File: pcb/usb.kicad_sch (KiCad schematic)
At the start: 4 parts

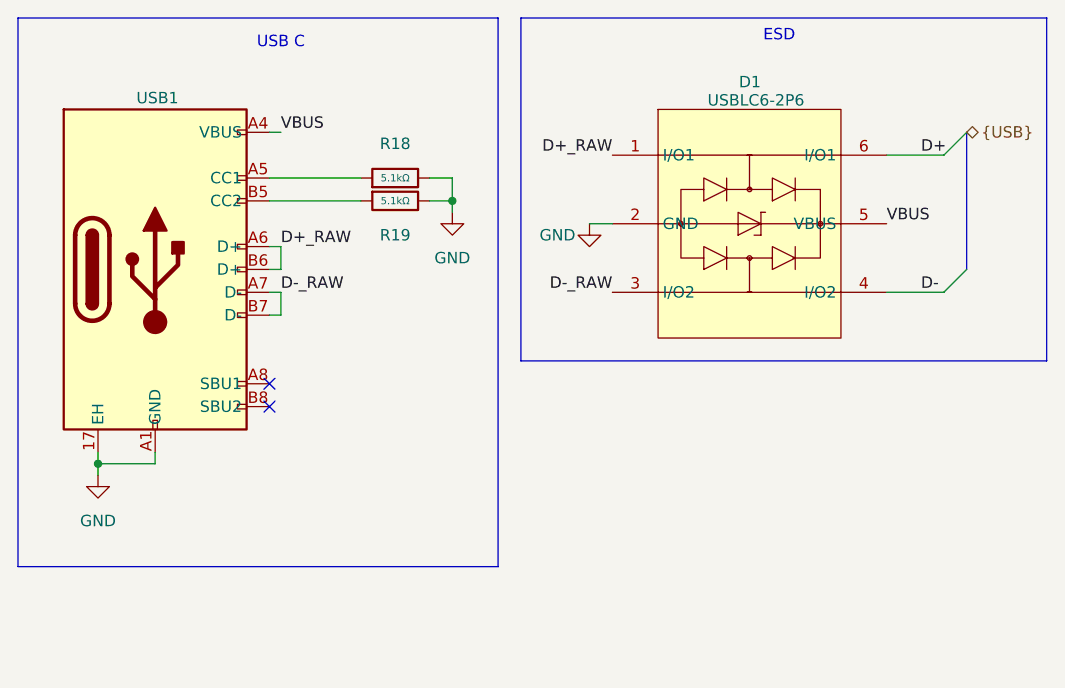
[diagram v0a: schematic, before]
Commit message: sch: add note about usb power
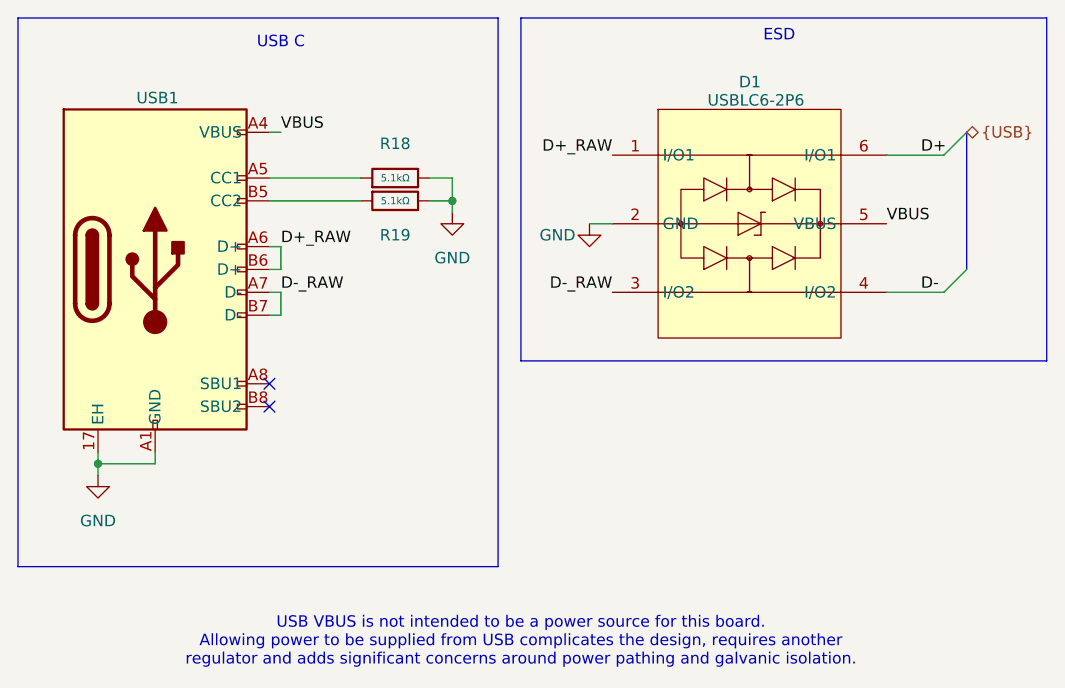
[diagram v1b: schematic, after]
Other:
- note added: "USB VBUS is not intended to be a power source for this board. Allowing power to be supplied from USB complicates the design, requires another regulator and adds significant concerns around power pathing and galvanic isolation."
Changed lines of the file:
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@@
+		)
+	)
+	(text "USB VBUS is not intended to be a power source for this board.\nAllowing power to be supplied from USB complicates the design, requires another\nregulator and adds significant concerns around power pathing and galvanic isolation."
+		(exclude_from_sim no)
+		(at 72.39 85.852 0)
+		(effects
+			(font
+				(size 1.27 1.27)
+			)
 		)
 	)

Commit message: pcb(mcu): route most of the esp
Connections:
- net D+_RAW renamed D_RAW+
- net D-_RAW renamed D_RAW-
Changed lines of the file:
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@@
 		)
 	)
-	(label "D-_RAW"
+	(label "D_RAW-"
 		(at 45.72 46.99 0)
 		(effects
@@
 		)
 	)
-	(label "D+_RAW"
+	(label "D_RAW+"
 		(at 45.72 41.91 0)
 		(effects
@@
 		)
 	)
-	(label "D-_RAW"
+	(label "D_RAW-"
 		(at 82.55 46.99 180)
 		(effects
@@
 		)
 	)
-	(label "D+_RAW"
+	(label "D_RAW+"
 		(at 82.55 31.75 180)
 		(effects
